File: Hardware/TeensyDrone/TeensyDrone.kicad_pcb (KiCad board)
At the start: 2 copper layers, 42 x 97.5 mm, 15 parts, among them J1 Conn_01x08, J2 Conn_01x08, U1 DEV-16771

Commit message: Adding Gerbers
Signed-off-by: lucas <mtglucas1@gmail.com>
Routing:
- added copper zone on F.Cu, net GND
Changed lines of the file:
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@@
 			(crossoutdnponfab yes)
 			(subtractmaskfromsilk no)
-			(outputformat 1)
+			(outputformat 4)
 			(mirror no)
 			(drillshape 0)
@@
 		(net 54)
 		(net_name "GND")
-		(layer "B.Cu")
+		(layers "F.Cu" "B.Cu")
 		(hatch edge 0.5)
 		(connect_pads

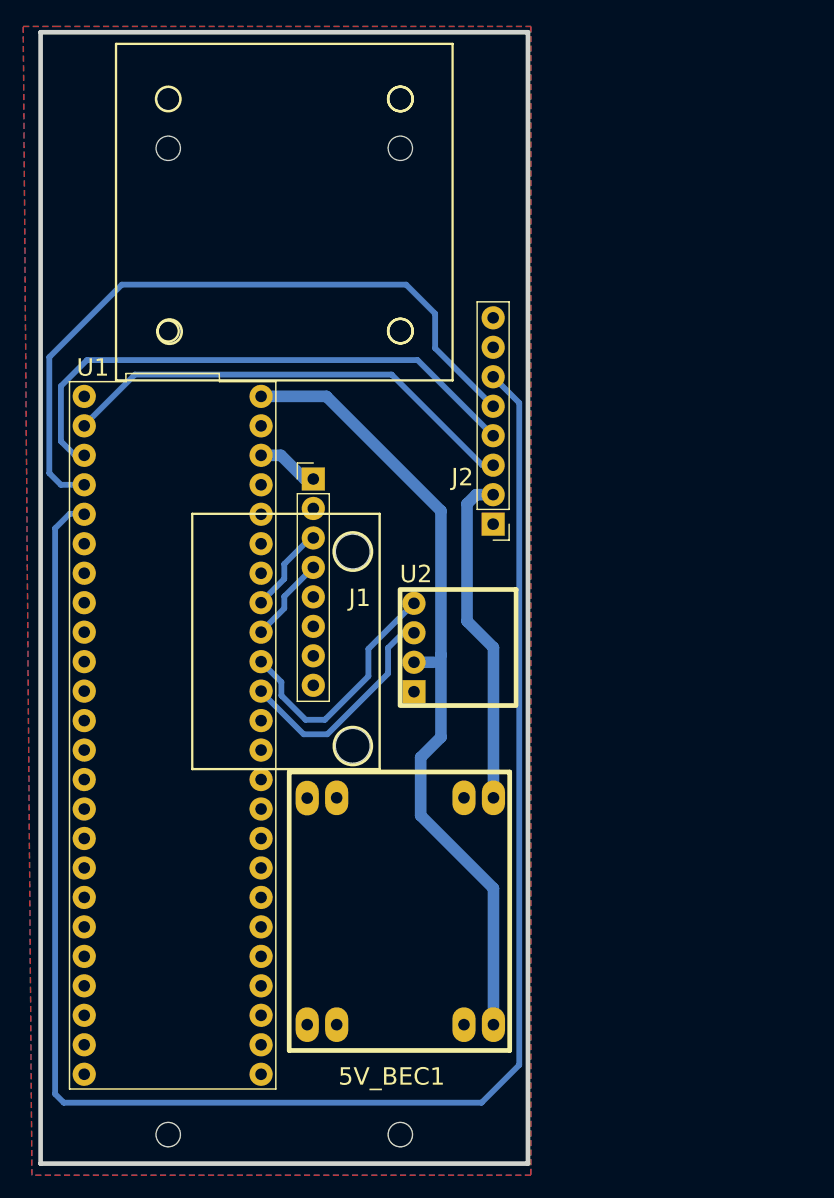
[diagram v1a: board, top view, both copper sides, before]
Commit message: Moved to Teensy 4.0 from 4.1
Signed-off-by: lucas <mtglucas1@gmail.com>
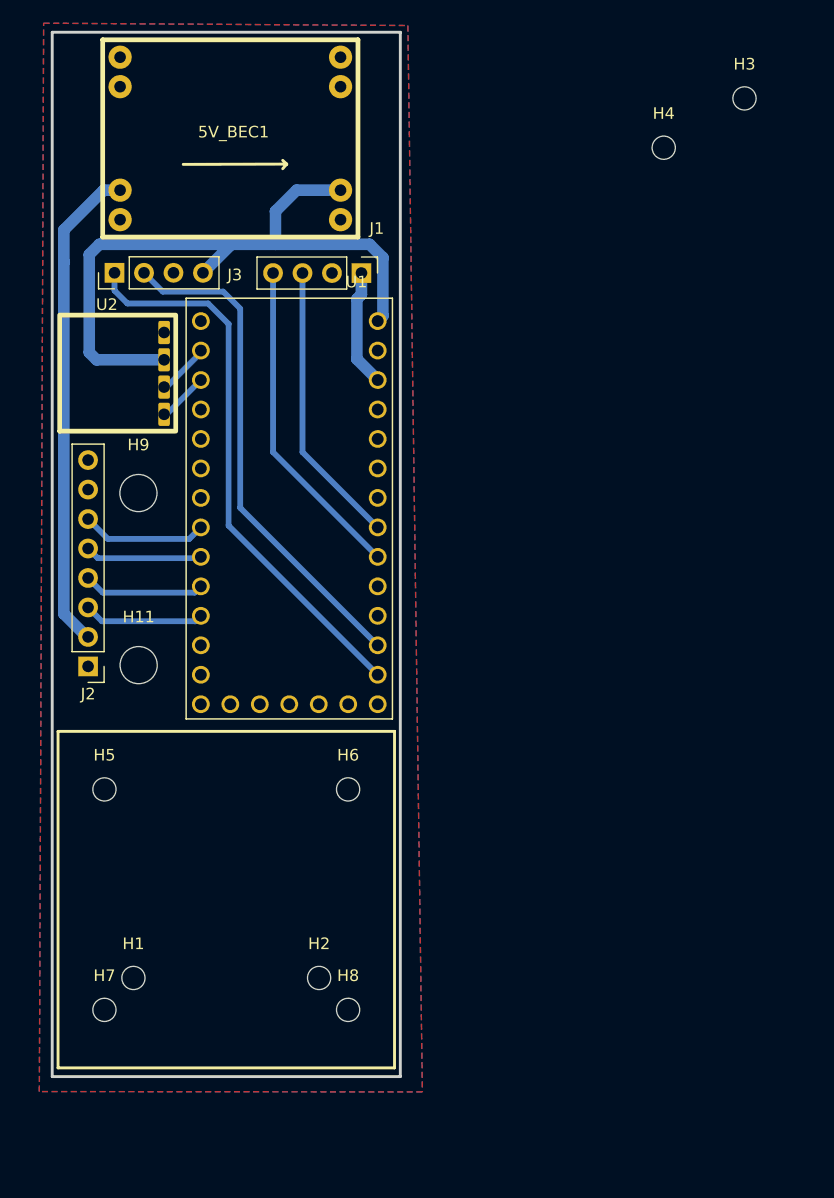
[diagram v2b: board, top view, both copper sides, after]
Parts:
- removed MountHole1, MountHole2, MountHole3, MountHole4: MountingHole_2.1mm, MountingHole:MountingHole_2.1mm
- removed MountingHoleAcc1, MountingHoleAcc2: , clipboard:ab9ca41b-535c-4e5d-965d-18f4c74ecc4b
- removed Mounting_hole_esc_1, Mounting_hole_esc_2, Mounting_hole_esc_3, Mounting_hole_esc_4: MNT, clipboard:cc0a7048-0dbf-4480-81d8-83834bec2c2a
- added H1: MountingHole, MountingHole:MountingHole_2mm, F.Cu at (32.0, 106.5)
- added H11: MountingHole, MountingHole:MountingHole_3.2mm_M3, F.Cu at (32.5, 79.5)
- added H2: MountingHole, MountingHole:MountingHole_2mm, F.Cu at (48.0, 106.5)
- added H3: MountingHole, MountingHole:MountingHole_2mm, F.Cu at (84.7, 30.7)
- added H4: MountingHole, MountingHole:MountingHole_2mm, F.Cu at (77.7, 35.0)
- added H5: MountingHole, MountingHole:MountingHole_2mm, F.Cu at (29.5, 90.2)
- added H6: MountingHole, MountingHole:MountingHole_2mm, F.Cu at (50.5, 90.2)
- added H7: MountingHole, MountingHole:MountingHole_2mm, F.Cu at (29.5, 109.2)
- added H8: MountingHole, MountingHole:MountingHole_2mm, F.Cu at (50.5, 109.2)
- added H9: MountingHole, MountingHole:MountingHole_3.2mm_M3, F.Cu at (32.4, 64.7)
- added J3: Conn_01x04, Connector_PinHeader_2.54mm:PinHeader_1x04_P2.54mm_Vertical, F.Cu at (30.4, 45.7)
- J1: value Conn_01x08 -> Conn_01x04; footprint Connector_PinHeader_2.54mm:PinHeader_1x08_P2.54mm_Vertical -> Connector_PinHeader_2.54mm:PinHeader_1x04_P2.54mm_Vertical
- U1: value DEV-16771 -> DEV-15583; footprint Teensy 4.1:MODULE_DEV-16771 -> DEV-15583:MODULE_DEV-15583
- moved 5V_BEC1 79.3 mm to (29.4, 25.6), turned to 0 degrees
- moved U2 41.6 mm to (25.6, 59.4), turned to 90 degrees
- moved J2 37.0 mm to (28.1, 79.7)
- moved U1 21.7 mm to (45.4, 66.4), turned to 0 degrees
- moved J1 18.2 mm to (51.6, 45.8), turned to -90 degrees
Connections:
- 5V_BEC1 pad 1: Net-(J2-VBat) -> GND
- 5V_BEC1 pad 3: GND -> Net-(J2-VBat)
- 5V_BEC1 pad 5: 5V -> GND
- 5V_BEC1 pad 7: GND -> Net-(J3-5V)
- J2 pad 3: Net-(J2-Servo1) -> Net-(J2-Pin_3)
- J2 pad 4: Net-(J2-Servo2) -> Net-(J2-Pin_4)
- J2 pad 5: Net-(J2-Servo3) -> Net-(J2-Pin_5)
- J2 pad 6: Net-(J2-Servo4) -> Net-(J2-Pin_6)
- U1 pad 0: Net-(J2-Servo1) -> Net-(U2-TX)
- U1 pad 1: Net-(J2-Servo2) -> Net-(U2-RX)
- U1 pad 14: unconnected-(U1-A0-Pad14) -> Net-(J3-RX)
- U1 pad 15: unconnected-(U1-A1-Pad15) -> Net-(J3-TX)
- U1 pad 16: Net-(U2-TX) -> unconnected-(U1-Pad16)
- U1 pad 17: Net-(U2-RX) -> unconnected-(U1-Pad17)
- U1 pad 2: Net-(J2-Servo3) -> unconnected-(U1-Pad2)
- U1 pad 3: Net-(J2-Servo4) -> unconnected-(U1-Pad3)
- U1 pad 6: unconnected-(U1-OUT1D-Pad6) -> Net-(J2-Pin_6)
- U1 pad 7: unconnected-(U1-RX2-Pad7) -> Net-(J2-Pin_5)
- U1 pad 8: unconnected-(U1-TX2-Pad8) -> Net-(J2-Pin_4)
- U1 pad 9: unconnected-(U1-OUT1C-Pad9) -> Net-(J2-Pin_3)
- U2 pad 2: 5V -> Net-(J3-5V)
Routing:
- net Net-(J2-Servo4): track 153.6 -> 0.00 mm
- net 5V: track 69.0 -> 0.00 mm
- net Net-(J2-Servo3): track 60.3 -> 0.00 mm
- net Net-(J3-5V): track 0.00 -> 59.6 mm
- net Net-(J3-RX): track 0.00 -> 48.1 mm
- net Net-(J2-Servo2): track 48.1 -> 0.00 mm
- net Net-(J3-TX): track 0.00 -> 43.5 mm
- net Net-(J2-Servo1): track 40.4 -> 0.00 mm
- net Net-(J1-SDA): track 7.46 -> 28.2 mm
- net Net-(U2-RX): track 21.8 -> 4.39 mm
- net Net-(J1-SCL): track 7.36 -> 24.6 mm
- net Net-(U2-TX): track 19.7 -> 4.58 mm
- net Net-(J2-VBat): track 28.9 -> 42.3 mm
- net Net-(J2-Pin_6): track 0.00 -> 10.8 mm
- net Net-(J2-Pin_4): track 0.00 -> 10.5 mm
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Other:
- board size 42 x 97.5 mm -> 30 x 90 mm
- board text added: "Board Cutout : 90mm x 30mm"
- board text added: "ESC Outline Mounted on Gummies above"
- board text added: "End of Drone"
- board text added: "Front of Drone"
- board text added: "IMU + ESC Both Not On Board, Mounted Above"

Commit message: Second iteration of PCB
Signed-off-by: lucas <mtglucas1@gmail.com>
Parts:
- moved J3 22.7 mm to (51.6, 37.7), turned to 0 degrees
- moved J1 13.1 mm to (38.6, 45.4)
- moved H4 11.7 mm to (89.4, 34.7)
- moved H3 4.55 mm to (89.2, 30.4)
- moved 5V_BEC1 3.60 mm to (25.8, 25.8)
- moved U1 0.24 mm to (45.2, 66.4)
- moved U2 0.12 mm to (25.6, 59.3)
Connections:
- net Net-(J2-VBat) renamed VBat
- J1 pad 1: Net-(J1-3.3V) -> Net-(J1-SDA)
- J1 pad 2: GND -> Net-(J1-SCL)
- J1 pad 3: Net-(J1-SCL) -> GND
- J1 pad 4: Net-(J1-SDA) -> 3.3V
- U1 pad 14: Net-(J3-RX) -> unconnected-(U1-Pad14)
- U1 pad 15: Net-(J3-TX) -> unconnected-(U1-Pad15)
- U1 pad 16: unconnected-(U1-Pad16) -> Net-(J1-SCL)
- U1 pad 17: unconnected-(U1-Pad17) -> Net-(J1-SDA)
- U1 pad 18: Net-(J1-SDA) -> unconnected-(U1-Pad18)
- U1 pad 19: Net-(J1-SCL) -> unconnected-(U1-Pad19)
- U1 pad 20: unconnected-(U1-Pad20) -> Net-(J3-RX)
- U1 pad 21: unconnected-(U1-Pad21) -> Net-(J3-TX)
- U1 pad 3.3V: Net-(J1-3.3V) -> 3.3V
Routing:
- net 3.3V: track 0.00 -> 44.0 mm
- net Net-(J3-TX): track 43.5 -> 28.4 mm
- net Net-(J3-RX): track 48.1 -> 33.6 mm
- net Net-(J1-SCL): track 24.6 -> 36.9 mm
- net Net-(J1-3.3V): track 10.1 -> 0.00 mm
- net Net-(J1-SDA): track 28.2 -> 33.3 mm
- net VBat: track 42.3 -> 40.0 mm
- net Net-(J3-5V): track 59.6 -> 61.2 mm
- net Net-(J2-Pin_4): track 10.5 -> 9.77 mm
- net Net-(J2-Pin_3): track 10.4 -> 9.77 mm
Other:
- board text added: "Only SMD Not THT"

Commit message: Done Hardware Section
Signed-off-by: lucas <mtglucas1@gmail.com>
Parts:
- removed H4: MountingHole, MountingHole:MountingHole_2mm
- removed U2: ~, ELRS_Lite_RX:ELRS_Lite_RX
- added J4: Conn_01x04, Connector_PinHeader_2.54mm:PinHeader_1x04_P2.54mm_Vertical, F.Cu at (29.0, 70.3)
- moved 5V_BEC1 59.9 mm to (37.5, 84.5), turned to 90 degrees
- moved H3 50.0 mm to (40.0, 39.5)
- moved J2 34.7 mm to (28.8, 45.0)
- moved U1 23.2 mm to (39.8, 43.9)
- moved J1 12.3 mm to (50.9, 44.9), turned to 180 degrees
- moved J3 11.0 mm to (50.9, 48.7)
- moved H9 2.29 mm to (33.6, 66.7)
- moved H11 2.29 mm to (33.6, 81.5)
- moved H5 0.50 mm to (29.5, 90.8)
- moved H6 0.50 mm to (50.5, 90.8)
- moved H7 0.50 mm to (29.5, 109.8)
- moved H8 0.50 mm to (50.5, 109.8)
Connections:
- net 3.3V renamed +3.3V
- net Net-(J3-5V) renamed 5V
- J1 pad 1: Net-(J1-SDA) -> IMU_SDA
- J1 pad 2: Net-(J1-SCL) -> IMU_SCL
- J3 pad 1: Net-(J3-RX) -> OF_RX
- J3 pad 2: Net-(J3-TX) -> OF_TX
- U1 pad 0: Net-(U2-TX) -> unconnected-(U1-Pad0)
- U1 pad 1: Net-(U2-RX) -> Net-(J2-Pin_6)
- U1 pad 14: unconnected-(U1-Pad14) -> ELRS_RX
- U1 pad 15: unconnected-(U1-Pad15) -> ELRS_TX
- U1 pad 16: Net-(J1-SCL) -> OF_TX
- U1 pad 17: Net-(J1-SDA) -> OF_RX
- U1 pad 18: unconnected-(U1-Pad18) -> IMU_SDA
- U1 pad 19: unconnected-(U1-Pad19) -> IMU_SCL
- U1 pad 2: unconnected-(U1-Pad2) -> Net-(J2-Pin_5)
- U1 pad 20: Net-(J3-RX) -> unconnected-(U1-Pad20)
- U1 pad 21: Net-(J3-TX) -> unconnected-(U1-Pad21)
- U1 pad 3: unconnected-(U1-Pad3) -> Net-(J2-Pin_4)
- U1 pad 4: unconnected-(U1-Pad4) -> Net-(J2-Pin_3)
- U1 pad 6: Net-(J2-Pin_6) -> unconnected-(U1-Pad6)
- U1 pad 7: Net-(J2-Pin_5) -> unconnected-(U1-Pad7)
- U1 pad 8: Net-(J2-Pin_4) -> unconnected-(U1-Pad8)
- U1 pad 9: Net-(J2-Pin_3) -> unconnected-(U1-Pad9)
- U1 pad G2: unconnected-(U1-GND-PadG2) -> GND
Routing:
- net VBat: track 40.0 -> 83.2 mm
- net +3.3V: track 44.0 -> 7.12 mm
- net Net-(J1-SCL): track 36.9 -> 0.00 mm
- net ELRS_TX: track 0.00 -> 35.1 mm
- net Net-(J3-RX): track 33.6 -> 0.00 mm
- net Net-(J1-SDA): track 33.3 -> 0.00 mm
- net ELRS_RX: track 0.00 -> 29.1 mm
- net Net-(J3-TX): track 28.4 -> 0.00 mm
- net 5V: track 61.2 -> 76.2 mm
- net Net-(J2-Pin_6): track 10.6 -> 3.43 mm
- net Net-(J2-Pin_5): track 9.98 -> 3.49 mm
- net Net-(J2-Pin_3): track 9.77 -> 3.49 mm
- net Net-(J2-Pin_4): track 9.77 -> 3.49 mm
- net IMU_SDA: track 0.00 -> 5.38 mm
- net OF_RX: track 0.00 -> 4.98 mm
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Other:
- board text added: "Access to USB Serial Port"
